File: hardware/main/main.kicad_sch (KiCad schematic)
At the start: 0 parts

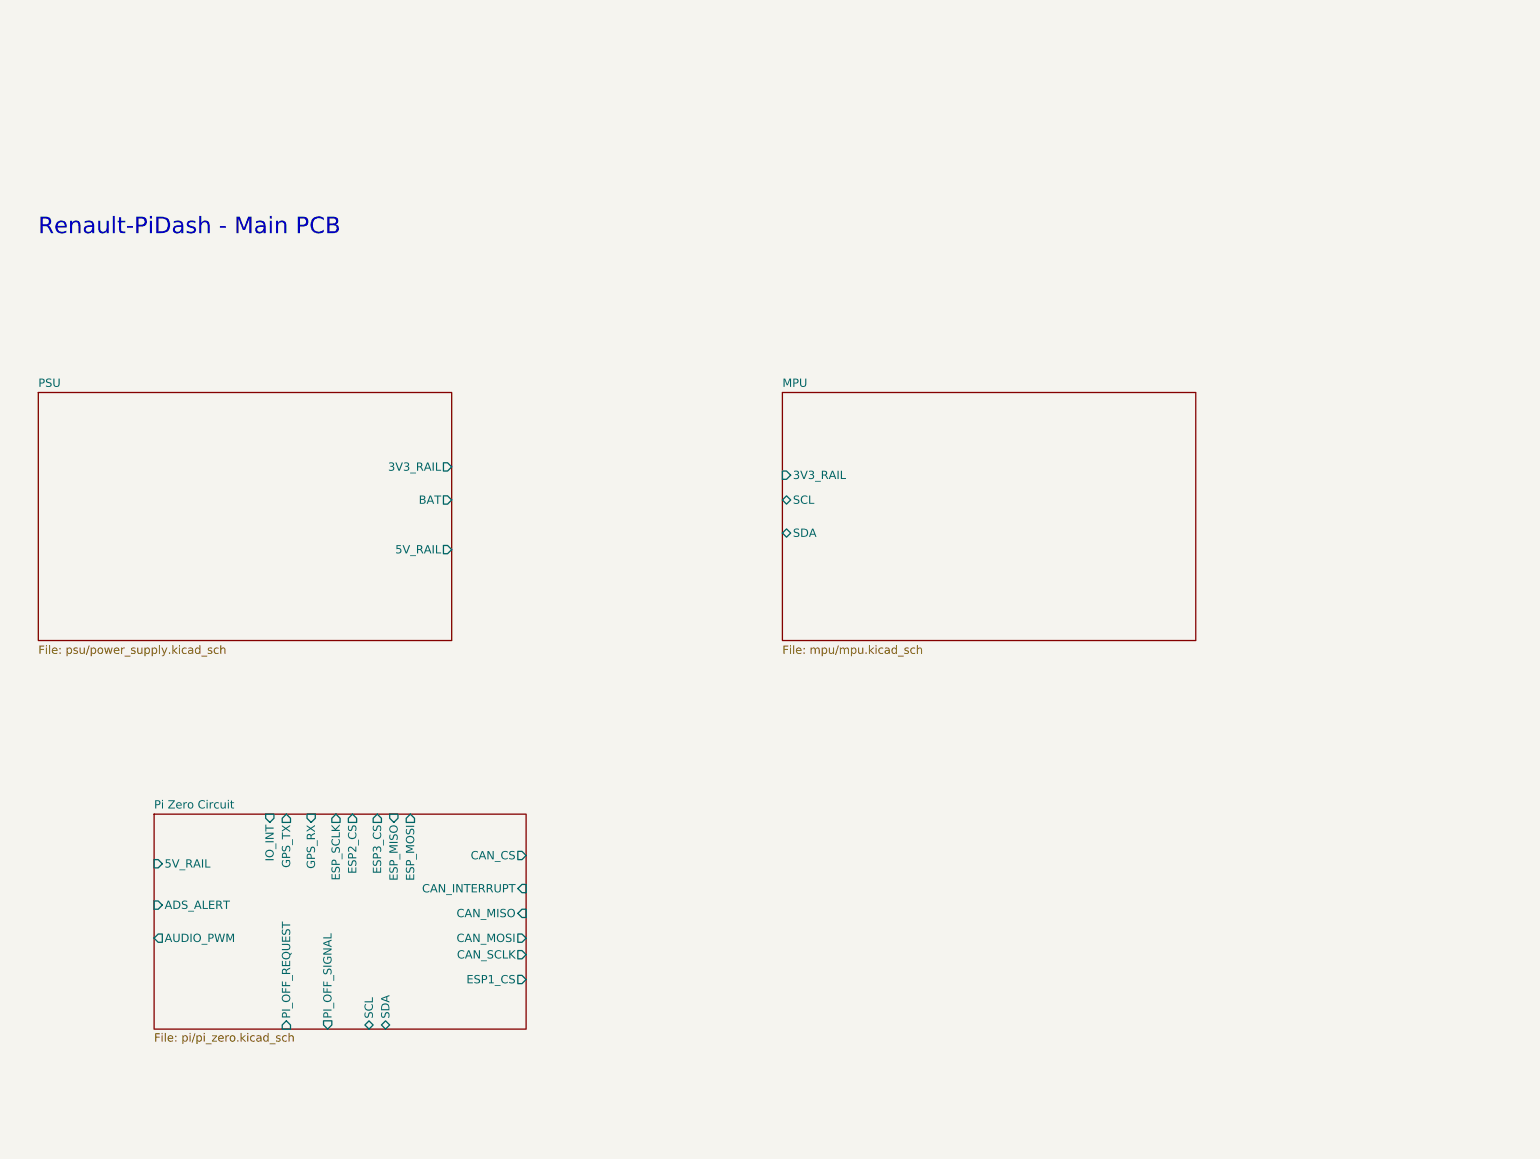
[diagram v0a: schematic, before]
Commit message: expanded main pcb schematics
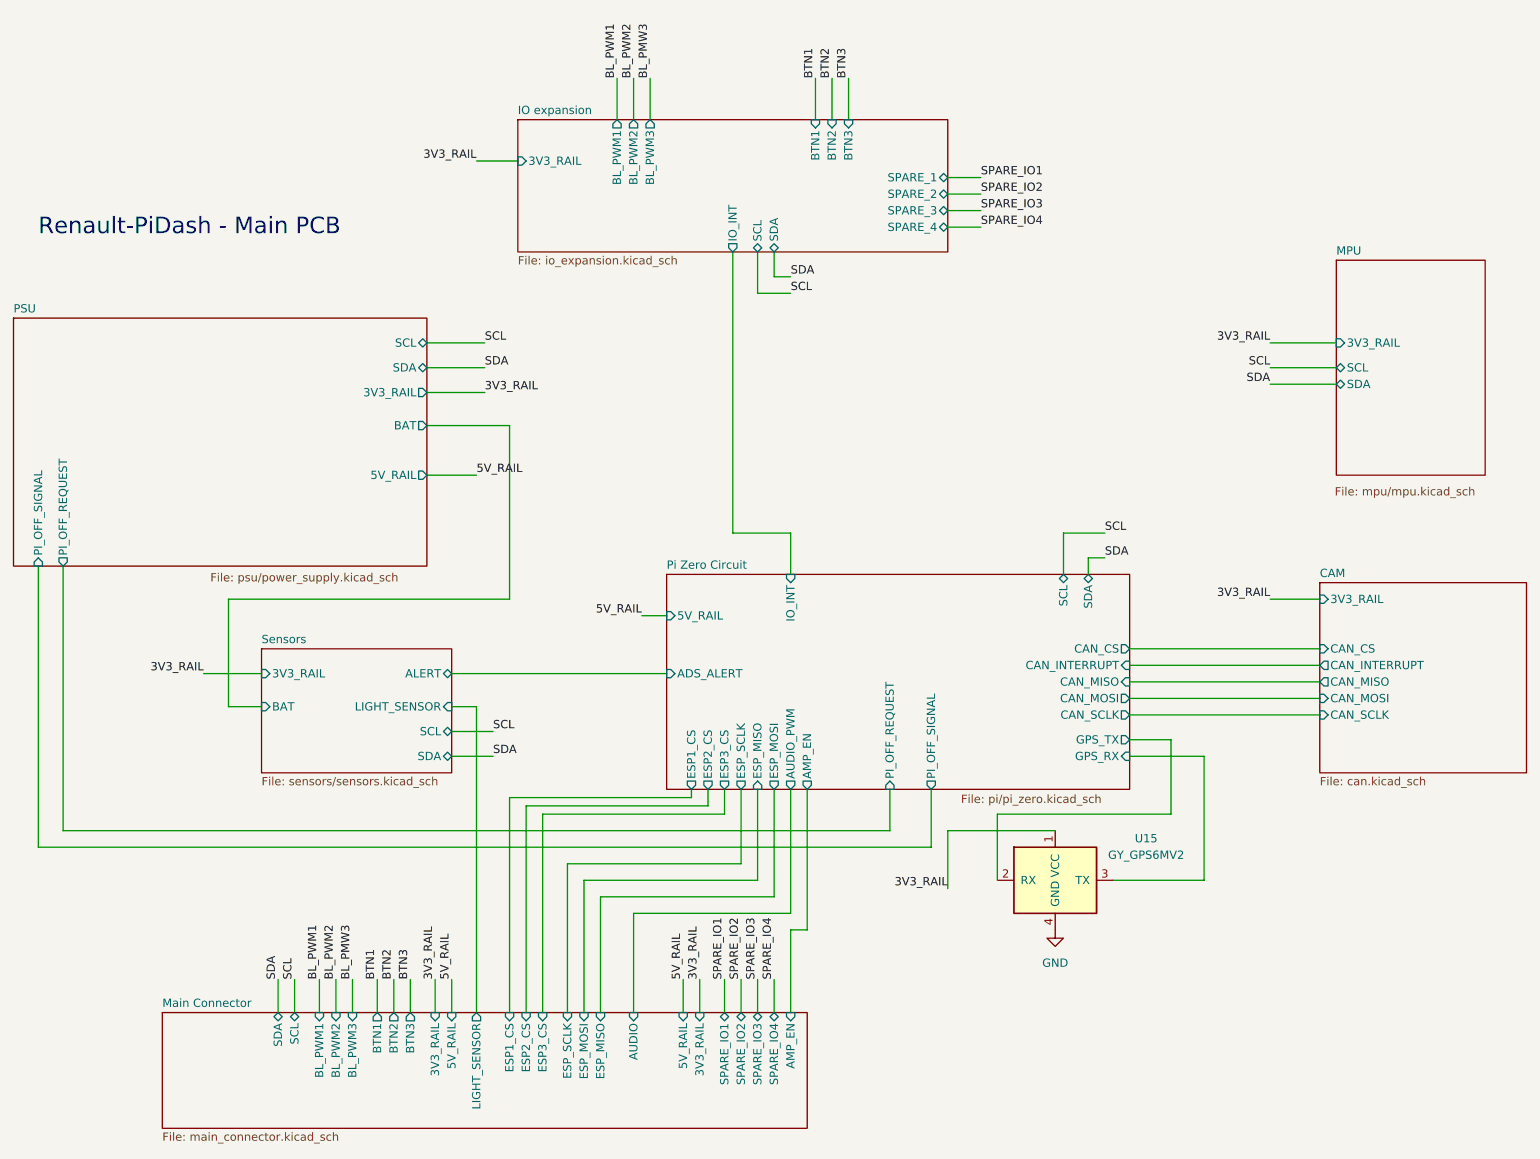
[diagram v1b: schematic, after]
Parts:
- added U15: GY_GPS6MV2, GY_GPS6MV2:GY_GPS6MV2_DirectWire_P2.54mm, symbol GY_GPS6MV2:GY_GPS6MV2
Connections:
- net Pi Zero Circuit/GPS_RX: now also U15.3 (TX)
- net Pi Zero Circuit/GPS_TX: now also U15.2 (RX)
- new net 3V3_RAIL: U15.1 (VCC)
- new net GND: U15.4 (GND)
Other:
- added sheet CAM (can.kicad_sch)
- added sheet IO expansion (io_expansion.kicad_sch)
- added sheet Main Connector (main_connector.kicad_sch)
- added sheet Sensors (sensors/sensors.kicad_sch)
- sheet PSU ports: added PI_OFF_REQUEST, PI_OFF_SIGNAL, SCL, SDA; removed none
- sheet Pi Zero Circuit ports: added AMP_EN; removed none

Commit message: fixed ERC issues
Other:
- sheet CAM renamed CAN
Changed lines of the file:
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@@
 	(wire
 		(pts
-			(xy 161.29 137.16) (xy 161.29 151.13)
+			(xy 161.29 137.16) (xy 161.29 149.86)
 		)
 		(stroke
@@
 	(wire
 		(pts
-			(xy 50.8 102.87) (xy 50.8 146.05)
-		)
-		(stroke
-			(width 0)
-			(type default)
-		)
-	)
-	(wire
-		(pts
 			(xy 153.67 137.16) (xy 153.67 139.7)
 		)
@@
 	(wire
 		(pts
-			(xy 166.37 137.16) (xy 166.37 156.21)
+			(xy 166.37 137.16) (xy 166.37 154.94)
 		)
 		(stroke
@@
 	(wire
 		(pts
-			(xy 54.61 102.87) (xy 54.61 143.51)
-		)
-		(stroke
-			(width 0)
-			(type default)
-		)
-	)
-	(wire
-		(pts
 			(xy 198.12 140.97) (xy 198.12 151.13)
 		)
@@
 	(wire
 		(pts
-			(xy 163.83 137.16) (xy 163.83 153.67)
+			(xy 163.83 137.16) (xy 163.83 152.4)
 		)
 		(stroke
@@
 	(wire
 		(pts
-			(xy 134.62 151.13) (xy 134.62 171.45)
+			(xy 134.62 149.86) (xy 134.62 171.45)
 		)
 		(stroke
@@
 	(wire
 		(pts
-			(xy 50.8 146.05) (xy 187.96 146.05)
+			(xy 54.61 102.87) (xy 54.61 107.95)
 		)
 		(stroke
@@
 	(wire
 		(pts
+			(xy 50.8 102.87) (xy 50.8 107.95)
+		)
+		(stroke
+			(width 0)
+			(type default)
+		)
+	)
+	(wire
+		(pts
 			(xy 151.13 137.16) (xy 151.13 138.43)
 		)
@@
 	(wire
 		(pts
-			(xy 163.83 153.67) (xy 137.16 153.67)
+			(xy 163.83 152.4) (xy 137.16 152.4)
 		)
 		(stroke
@@
 	(wire
 		(pts
-			(xy 187.96 146.05) (xy 187.96 137.16)
-		)
-		(stroke
-			(width 0)
-			(type default)
-		)
-	)
-	(wire
-		(pts
 			(xy 107.95 166.37) (xy 107.95 171.45)
 		)
@@
 	(wire
 		(pts
-			(xy 137.16 153.67) (xy 137.16 171.45)
+			(xy 137.16 152.4) (xy 137.16 171.45)
 		)
 		(stroke
@@
 	(wire
 		(pts
-			(xy 54.61 143.51) (xy 181.61 143.51)
-		)
-		(stroke
-			(width 0)
-			(type default)
-		)
-	)
-	(wire
-		(pts
 			(xy 240.03 72.39) (xy 250.19 72.39)
 		)
@@
 	(wire
 		(pts
-			(xy 158.75 137.16) (xy 158.75 148.59)
+			(xy 158.75 137.16) (xy 158.75 147.32)
 		)
 		(stroke
@@
 	(wire
 		(pts
-			(xy 161.29 151.13) (xy 134.62 151.13)
+			(xy 161.29 149.86) (xy 134.62 149.86)
 		)
 		(stroke
@@
 	(wire
 		(pts
-			(xy 158.75 148.59) (xy 132.08 148.59)
-		)
-		(stroke
-			(width 0)
-			(type default)
-		)
-	)
-	(wire
-		(pts
-			(xy 190.5 152.4) (xy 190.5 143.51)
+			(xy 158.75 147.32) (xy 132.08 147.32)
+		)
+		(stroke
+			(width 0)
+			(type default)
+		)
+	)
+	(wire
+		(pts
+			(xy 196.85 158.75) (xy 196.85 143.51)
 		)
 		(stroke
@@
 	(wire
 		(pts
-			(xy 142.24 156.21) (xy 142.24 171.45)
+			(xy 140.97 154.94) (xy 140.97 171.45)
 		)
 		(stroke
@@
 	(wire
 		(pts
-			(xy 132.08 148.59) (xy 132.08 171.45)
+			(xy 132.08 147.32) (xy 132.08 171.45)
 		)
 		(stroke
@@
 	(wire
 		(pts
-			(xy 190.5 143.51) (xy 207.01 143.51)
+			(xy 196.85 143.51) (xy 207.01 143.51)
 		)
 		(stroke
@@
 	(wire
 		(pts
+			(xy 187.96 137.16) (xy 187.96 143.51)
+		)
+		(stroke
+			(width 0)
+			(type default)
+		)
+	)
+	(wire
+		(pts
 			(xy 166.37 58.42) (xy 163.83 58.42)
 		)
@@
 	(wire
 		(pts
-			(xy 166.37 156.21) (xy 142.24 156.21)
+			(xy 166.37 154.94) (xy 140.97 154.94)
 		)
 		(stroke
@@
 		)
 	)
+	(label "PI_OFF_SIGNAL"
+		(at 187.96 143.51 270)
+		(effects
+			(font
+				(size 1.27 1.27)
+			)
+			(justify right bottom)
+		)
+	)
 	(label "SPARE_IO1"
 		(at 195.58 43.18 0)
@@
 		)
 	)
+	(label "PI_OFF_REQUEST"
+		(at 181.61 143.51 270)
+		(effects
+			(font
+				(size 1.27 1.27)
+			)
+			(justify right bottom)
+		)
+	)
 	(label "5V_RAIL"
 		(at 149.86 166.37 90)
@@
 		)
 	)
+	(label "PI_OFF_REQUEST"
+		(at 54.61 107.95 270)
+		(effects
+			(font
+				(size 1.27 1.27)
+			)
+			(justify right bottom)
+		)
+	)
 	(label "BTN2"
 		(at 172.72 27.94 90)
@@
 	)
 	(label "3V3_RAIL"
-		(at 190.5 152.4 180)
+		(at 196.85 158.75 180)
 		(effects
 			(font
@@
 			)
 			(justify left bottom)
+		)
+	)
+	(label "PI_OFF_SIGNAL"
+		(at 50.8 107.95 270)
+		(effects
+			(font
+				(size 1.27 1.27)
+			)
+			(justify right bottom)
 		)
 	)
@@
 		)
 		(pin "AUDIO" input
-			(at 142.24 171.45 90)
+			(at 140.97 171.45 90)
 			(effects
 				(font
@@
 			(color 0 0 0 0)
 		)
-		(property "Sheetname" "CAM"
+		(property "Sheetname" "CAN"
 			(at 247.65 104.6984 0)
 			(show_name no)
